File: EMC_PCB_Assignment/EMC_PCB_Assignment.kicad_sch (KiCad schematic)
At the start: 81 parts, among them IC1 LT8636JV#PBF, IC2 LP2985AIM5-3.0_NOPB, IC3 ATMEGA16U2-MU, IC4 ATMEGA328P-PU, IC5 OPA4350UA, J1 3x2 Connector, J10 16 MHz, J2 3x2 Connector, J3 Header 8, J4 61300821121, J5 Header 10, J6 61300421121, J7 USB_B_Micro, J8 Power Connector, J9 16 MHz

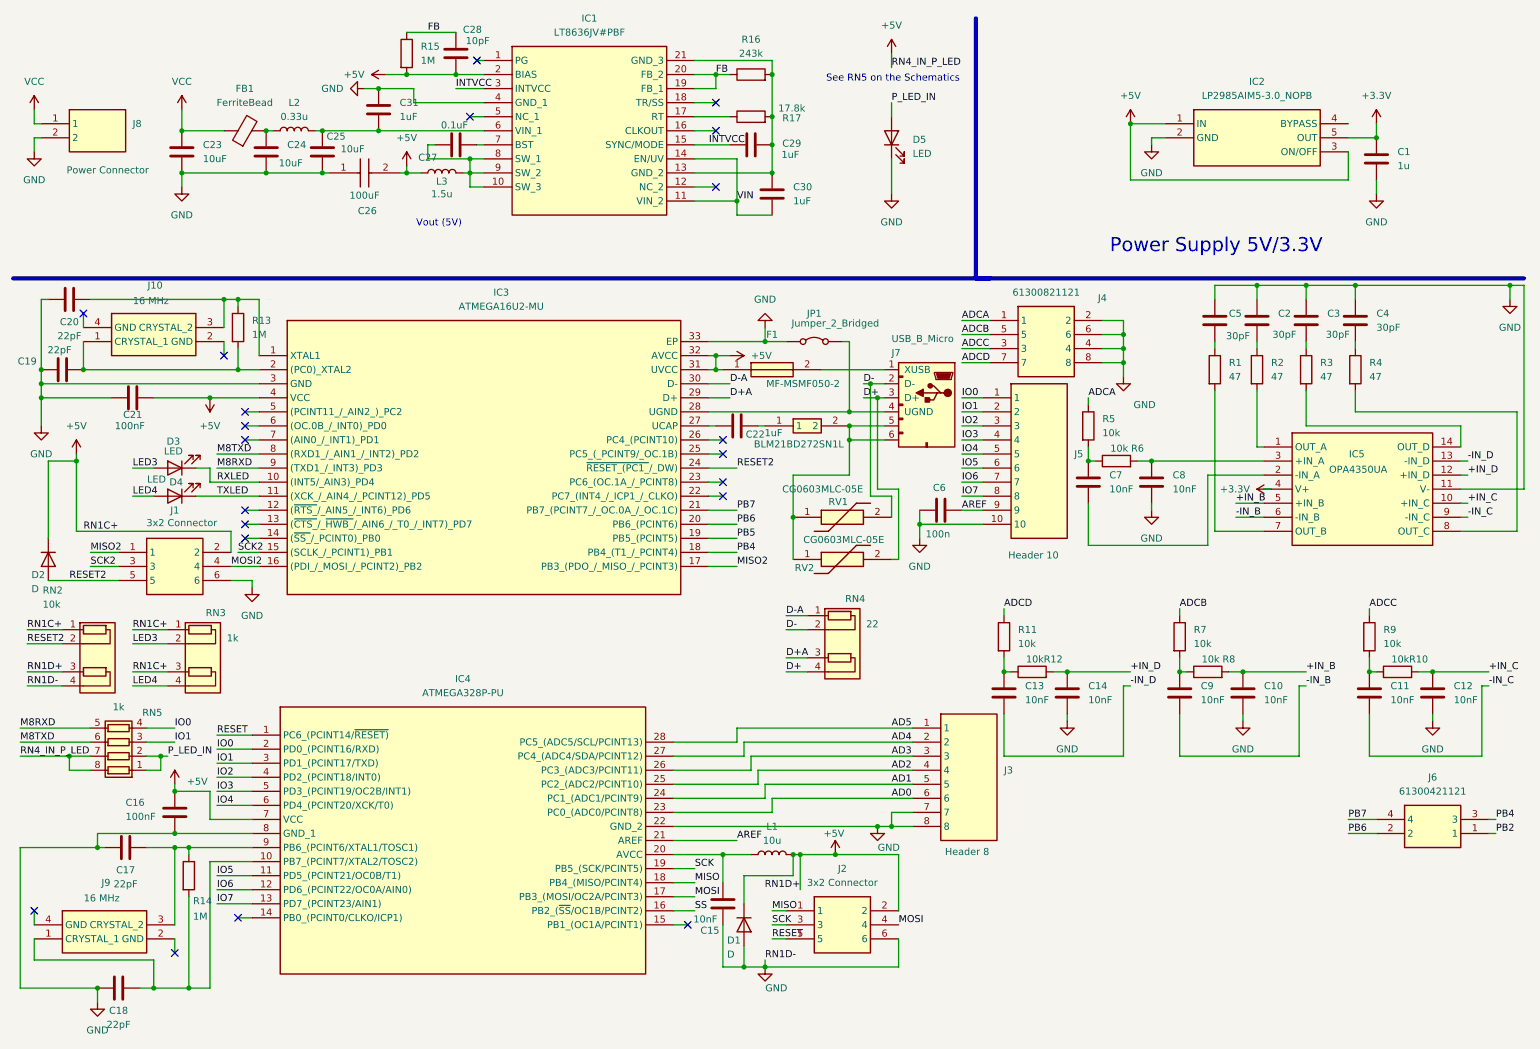
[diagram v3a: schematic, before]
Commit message: Added netlists and constraints to schematic
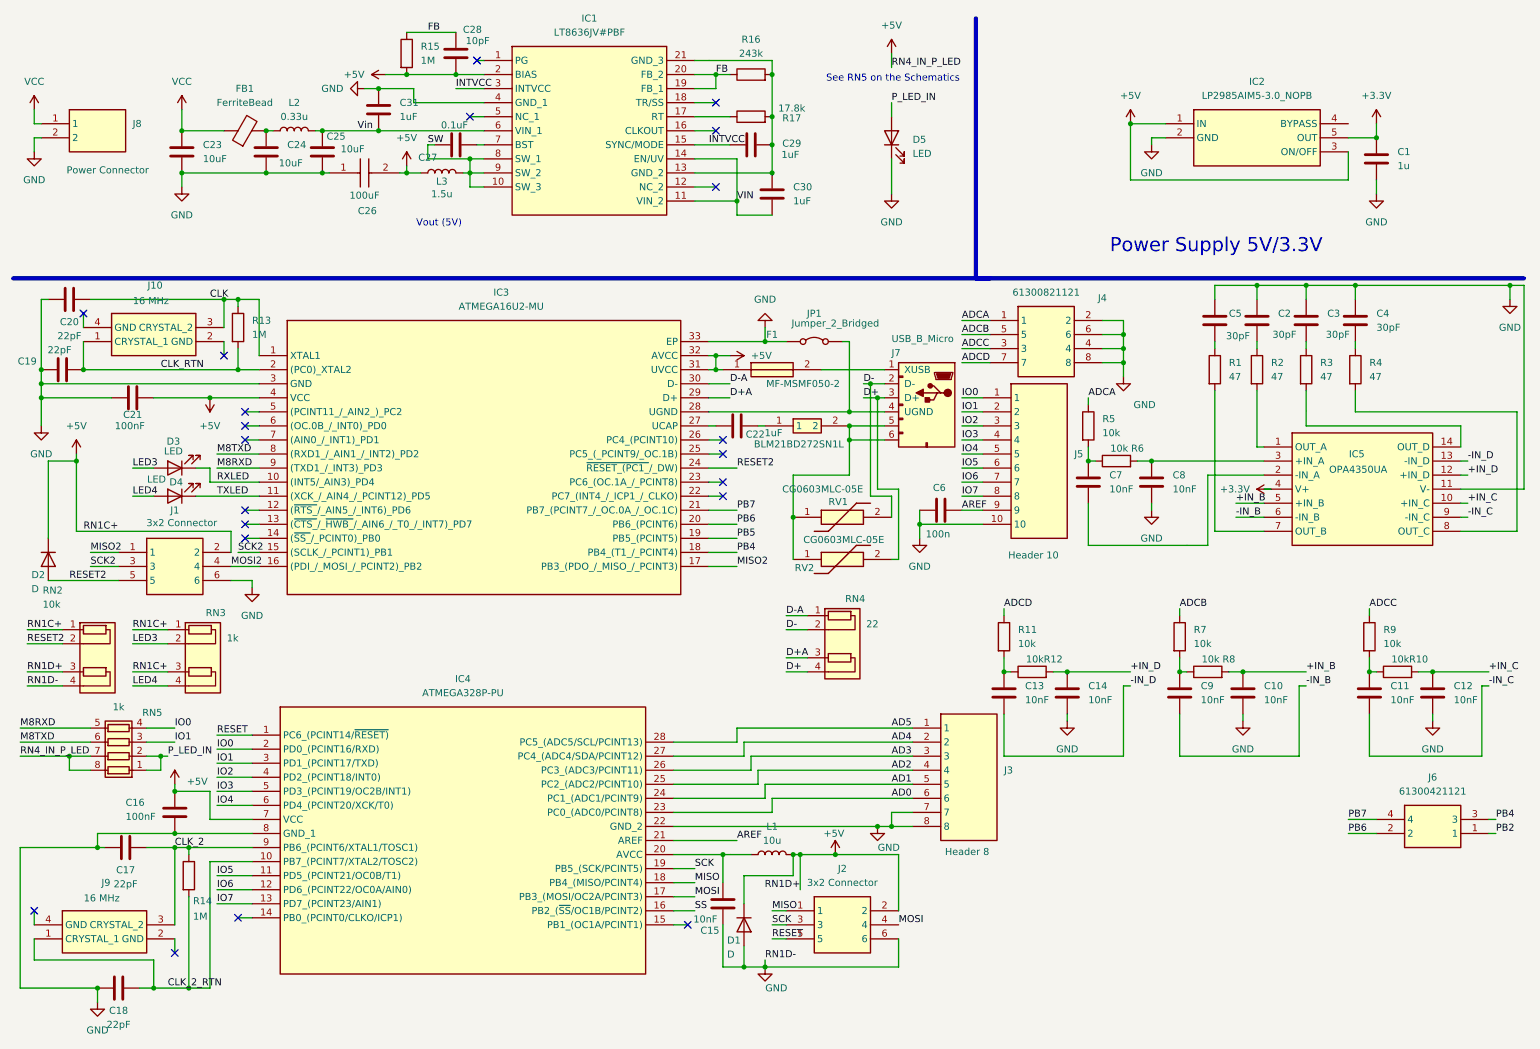
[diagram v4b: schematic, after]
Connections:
- net CLK_2_RTN: now reaches C18.2, IC4.10 (PB7_(PCINT7/XTAL2/TOSC2)), J9.1 (CRYSTAL_1), R14.2
- net CLK_2: now reaches C17.2, IC4.9 (PB6_(PCINT6/XTAL1/TOSC1)), J9.3 (CRYSTAL_2), R14.1
- net SW: now reaches C27.1, IC1.10 (SW_3), IC1.8 (SW_1), IC1.9 (SW_2), L3.2
- net Net1: now reaches C29.2, C30.2, IC1.13 (GND_2), IC1.21 (GND_3), R16.2, R17.2
- net Vin: now reaches C25.1, C31.2, IC1.6 (VIN_1), L2.2
- net CLK_RTN: now reaches C19.2, IC3.2 ((PC0)_XTAL2), J10.1 (CRYSTAL_1), R13.2
- net R9_Net: now reaches C11.1, R10.1, R9.2
- net AVCC_Net: now reaches C15.1, IC4.20 (AVCC), L1.1
- net R5_Net: now reaches C7.1, R5.2, R6.1
- net R6_Net: now reaches C8.1, IC5.3 (+IN_A), R6.2
- net R7_Net: now reaches C9.1, R7.2, R8.1
- net R2_Net: now reaches IC5.1 (OUT_A), R2.2
- net R3_Net: now reaches IC5.14 (OUT_D), R3.2
- net C7_Net: now reaches C7.2, IC5.2 (-IN_A)
- net R1_Net: now reaches IC5.7 (OUT_B), R1.2
- net R4_Net: now reaches IC5.8 (OUT_C), R4.2
- net R11_Net: now reaches C13.1, R11.2, R12.1
- net CLK: now reaches C20.2, IC3.1 (XTAL1), J10.3 (CRYSTAL_2), R13.1
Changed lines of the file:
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@@
+		)
+	)
+	(label "CLK"
+		(at 46.99 63.5 0)
+		(fields_autoplaced yes)
+		(effects
+			(font
+				(size 1.27 1.27)
+			)
+			(justify left bottom)
 		)
 	)
@@
 		)
 	)
+	(label "R6_Net"
+		(at 222.25 92.71 0)
+		(fields_autoplaced yes)
+		(effects
+			(font
+				(size 0.0254 0.0254)
+			)
+			(justify left bottom)
+		)
+	)
+	(label "R7_Net"
+		(at 222.25 130.81 0)
+		(fields_autoplaced yes)
+		(effects
+			(font
+				(size 0.0254 0.0254)
+			)
+			(justify left bottom)
+		)
+	)
 	(label "SCK2"
 		(at 52.07 109.22 0)
@@
 		)
 	)
+	(label "R9_Net"
+		(at 256.54 130.81 0)
+		(fields_autoplaced yes)
+		(effects
+			(font
+				(size 0.0254 0.0254)
+			)
+			(justify left bottom)
+		)
+	)
 	(label "ADCA"
 		(at 205.74 81.28 0)
@@
 		)
 	)
+	(label "R2_Net"
+		(at 236.22 85.09 0)
+		(fields_autoplaced yes)
+		(effects
+			(font
+				(size 0.0254 0.0254)
+			)
+			(justify left bottom)
+		)
+	)
 	(label "M8TXD"
 		(at 48.26 91.44 0)
@@
 		)
 	)
+	(label "AVCC_Net"
+		(at 140.97 163.83 0)
+		(fields_autoplaced yes)
+		(effects
+			(font
+				(size 0.0254 0.0254)
+			)
+			(justify left bottom)
+		)
+	)
 	(label "IO7"
 		(at 182.88 99.06 0)
@@
 		)
 	)
+	(label "R4_Net"
+		(at 256.54 83.82 0)
+		(fields_autoplaced yes)
+		(effects
+			(font
+				(size 0.0254 0.0254)
+			)
+			(justify left bottom)
+		)
+	)
+	(label "Net1"
+		(at 137.16 20.32 0)
+		(fields_autoplaced yes)
+		(effects
+			(font
+				(size 0.0254 0.0254)
+			)
+			(justify left bottom)
+		)
+	)
 	(label "ADCC"
 		(at 182.88 72.39 0)
@@
 		)
 	)
+	(label "R3_Net"
+		(at 245.11 83.82 0)
+		(fields_autoplaced yes)
+		(effects
+			(font
+				(size 0.0254 0.0254)
+			)
+			(justify left bottom)
+		)
+	)
 	(label "ADCD"
 		(at 182.88 74.93 0)
@@
 		)
 	)
+	(label "Vin"
+		(at 73.66 33.02 0)
+		(fields_autoplaced yes)
+		(effects
+			(font
+				(size 1.27 1.27)
+			)
+			(justify left bottom)
+		)
+	)
 	(label "+IN_C"
 		(at 278.13 130.81 0)
@@
 		)
 	)
+	(label "R5_Net"
+		(at 205.74 92.71 0)
+		(fields_autoplaced yes)
+		(effects
+			(font
+				(size 0.0254 0.0254)
+			)
+			(justify left bottom)
+		)
+	)
 	(label "FB"
 		(at 138.43 22.86 0)
@@
 		)
 	)
+	(label "CLK_2"
+		(at 40.64 162.56 0)
+		(fields_autoplaced yes)
+		(effects
+			(font
+				(size 1.27 1.27)
+			)
+			(justify left bottom)
+		)
+	)
 	(label "PB2"
 		(at 279.4 160.02 0)
@@
 		)
 	)
+	(label "R11_Net"
+		(at 190.5 130.81 0)
+		(fields_autoplaced yes)
+		(effects
+			(font
+				(size 0.0254 0.0254)
+			)
+			(justify left bottom)
+		)
+	)
 	(label "SS"
 		(at 134.62 173.99 0)
@@
 		)
 	)
+	(label "SW"
+		(at 86.36 35.56 0)
+		(fields_autoplaced yes)
+		(effects
+			(font
+				(size 1.27 1.27)
+			)
+			(justify left bottom)
+		)
+	)
 	(label "-IN_D"
 		(at 213.36 133.35 0)
@@
 		)
 	)
+	(label "CLK_RTN"
+		(at 38.1 76.2 0)
+		(fields_autoplaced yes)
+		(effects
+			(font
+				(size 1.27 1.27)
+			)
+			(justify left bottom)
+		)
+	)
+	(label "CLK_2_RTN"
+		(at 39.37 187.96 0)
+		(fields_autoplaced yes)
+		(effects
+			(font
+				(size 1.27 1.27)
+			)
+			(justify left bottom)
+		)
+	)
 	(label "D+A"
 		(at 140.97 81.28 0)
@@
 		)
 	)
+	(label "R1_Net"
+		(at 228.6 86.36 0)
+		(fields_autoplaced yes)
+		(effects
+			(font
+				(size 0.0254 0.0254)
+			)
+			(justify left bottom)
+		)
+	)
 	(label "SCK2"
 		(at 25.4 111.76 0)
@@
 			)
 			(justify left bottom)
+		)
+	)
+	(label "C7_Net"
+		(at 223.52 107.95 0)
+		(fields_autoplaced yes)
+		(effects
+			(font
+				(size 0.0254 0.0254)
+			)
+			(justify left bottom)
